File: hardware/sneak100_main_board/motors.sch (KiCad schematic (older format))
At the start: 16 parts, among them J1 Conn_01x06, J2 Conn_01x06, J3 Conn_01x06, J4 Conn_01x06, U1 DRV8835, U2 DRV8835, U3 DRV8835, U4 DRV8835

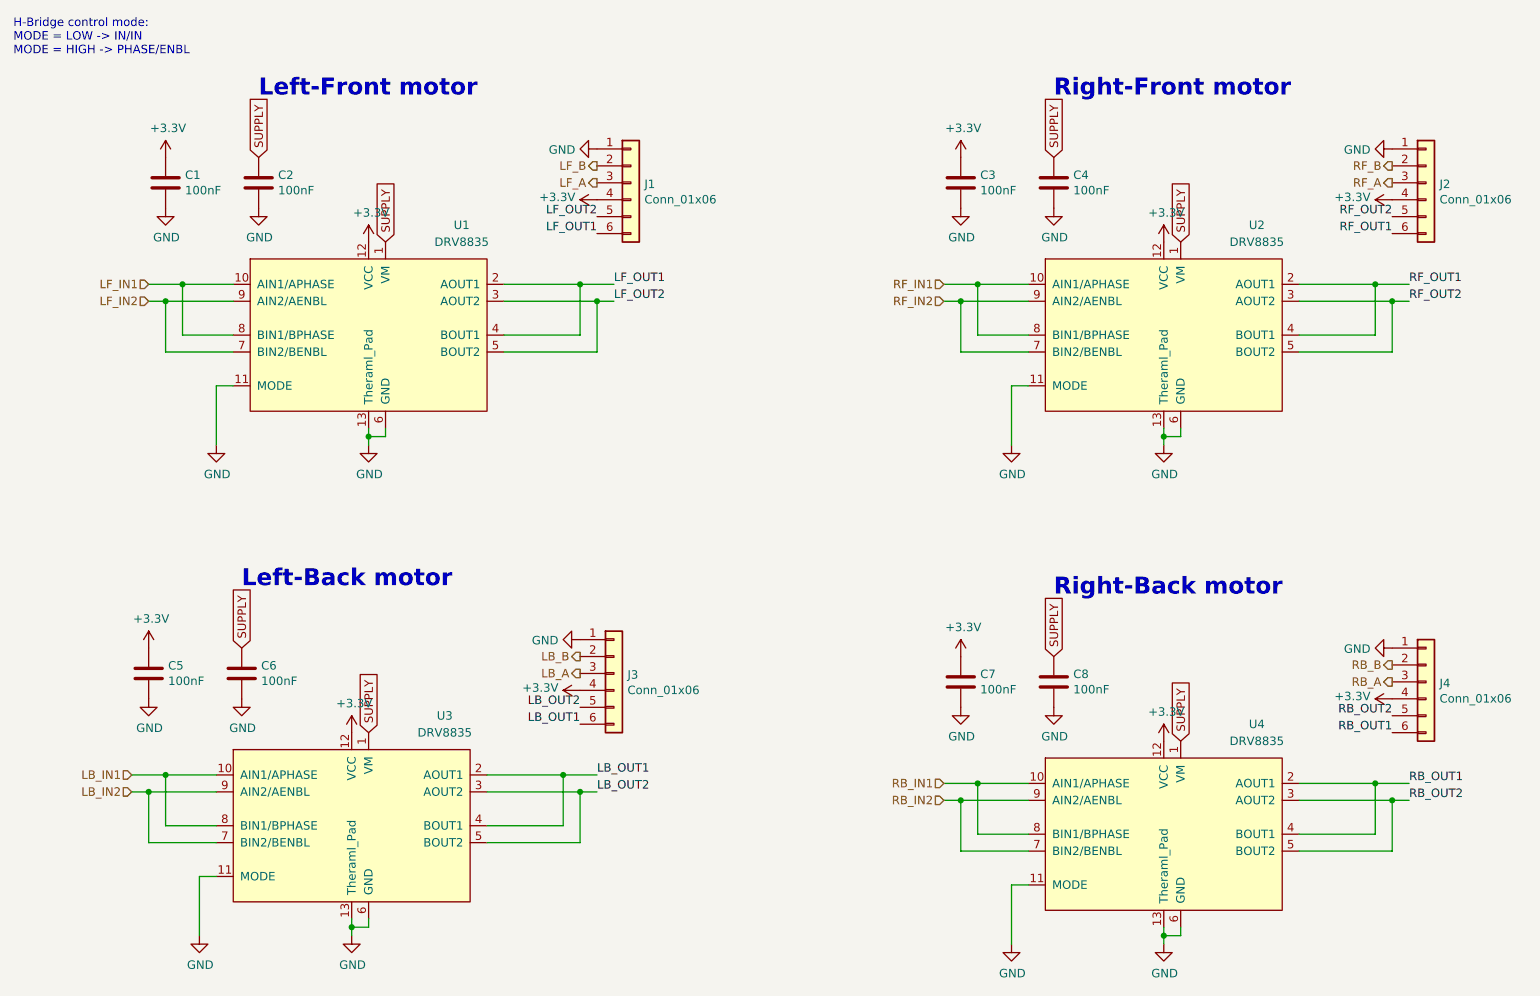
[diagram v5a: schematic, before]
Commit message: PCB first full layout
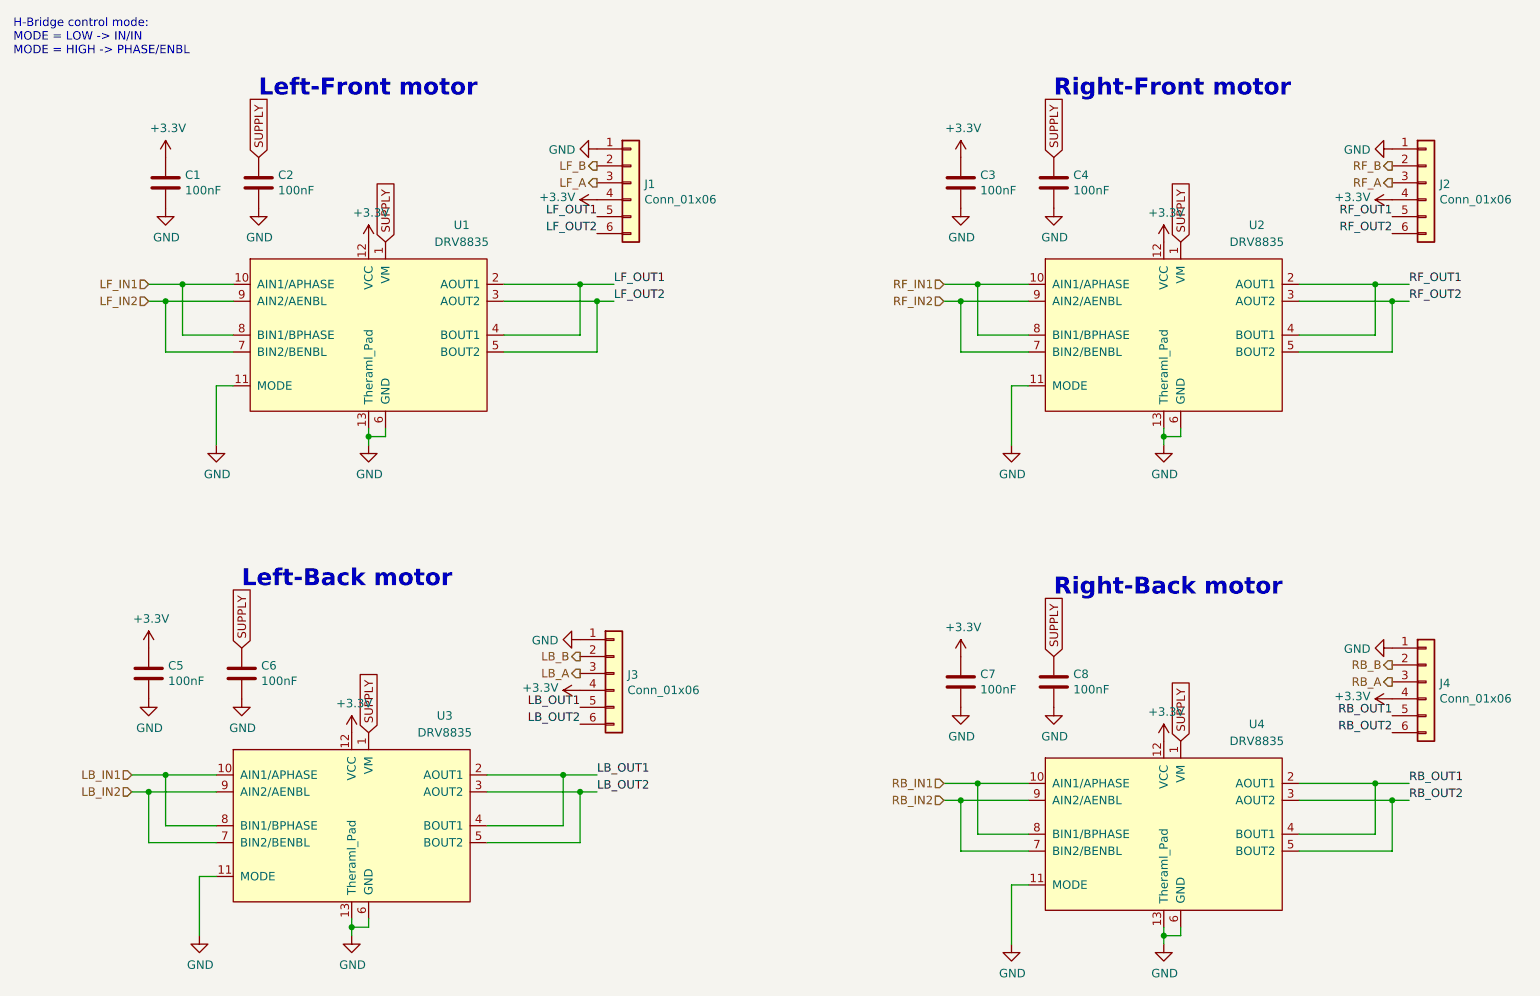
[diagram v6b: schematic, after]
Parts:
- J1, J2, J3, J4: footprint Connector_JST:JST_PH_S6B-PH-K_1x06_P2.00mm_Horizontal -> Connector_PinSocket_2.54mm:PinSocket_1x06_P2.54mm_Horizontal
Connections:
- net LB_OUT1: now also J3.5 (Pin_5); no longer J3.6 (Pin_6)
- net LB_OUT2: now also J3.6 (Pin_6); no longer J3.5 (Pin_5)
- net LF_OUT1: now also J1.5 (Pin_5); no longer J1.6 (Pin_6)
- net LF_OUT2: now also J1.6 (Pin_6); no longer J1.5 (Pin_5)
- net RB_OUT1: now also J4.5 (Pin_5); no longer J4.6 (Pin_6)
- net RB_OUT2: now also J4.6 (Pin_6); no longer J4.5 (Pin_5)
- net RF_OUT1: now also J2.5 (Pin_5); no longer J2.6 (Pin_6)
- net RF_OUT2: now also J2.6 (Pin_6); no longer J2.5 (Pin_5)
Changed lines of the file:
@@
 F 0 "J1" H 4630 1642 50  0000 L CNN
 F 1 "Conn_01x06" H 4630 1551 50  0000 L CNN
-F 2 "Connector_JST:JST_PH_S6B-PH-K_1x06_P2.00mm_Horizontal" H 4550 1650 50  0001 C CNN
+F 2 "Connector_PinSocket_2.54mm:PinSocket_1x06_P2.54mm_Horizontal" H 4550 1650 50  0001 C CNN
 F 3 "~" H 4550 1650 50  0001 C CNN
 	1    4550 1650
@@
 	0    -1   -1   0
 $EndComp
+Text Label 4350 1850 2    50   ~ 0
+LF_OUT1
 Text Label 4350 1950 2    50   ~ 0
-LF_OUT1
-Text Label 4350 1850 2    50   ~ 0
 LF_OUT2
 Text HLabel 4350 1650 0    50   Output ~ 0
@@
 F 0 "J2" H 9330 1642 50  0000 L CNN
 F 1 "Conn_01x06" H 9330 1551 50  0000 L CNN
-F 2 "Connector_JST:JST_PH_S6B-PH-K_1x06_P2.00mm_Horizontal" H 9250 1650 50  0001 C CNN
+F 2 "Connector_PinSocket_2.54mm:PinSocket_1x06_P2.54mm_Horizontal" H 9250 1650 50  0001 C CNN
 F 3 "~" H 9250 1650 50  0001 C CNN
 	1    9250 1650
@@
 	0    -1   -1   0
 $EndComp
+Text Label 9050 1850 2    50   ~ 0
+RF_OUT1
 Text Label 9050 1950 2    50   ~ 0
-RF_OUT1
-Text Label 9050 1850 2    50   ~ 0
 RF_OUT2
 Text HLabel 9050 1650 0    50   Output ~ 0
@@
 F 0 "J3" H 4530 4542 50  0000 L CNN
 F 1 "Conn_01x06" H 4530 4451 50  0000 L CNN
-F 2 "Connector_JST:JST_PH_S6B-PH-K_1x06_P2.00mm_Horizontal" H 4450 4550 50  0001 C CNN
+F 2 "Connector_PinSocket_2.54mm:PinSocket_1x06_P2.54mm_Horizontal" H 4450 4550 50  0001 C CNN
 F 3 "~" H 4450 4550 50  0001 C CNN
 	1    4450 4550
@@
 	0    -1   -1   0
 $EndComp
+Text Label 4250 4750 2    50   ~ 0
+LB_OUT1
 Text Label 4250 4850 2    50   ~ 0
-LB_OUT1
-Text Label 4250 4750 2    50   ~ 0
 LB_OUT2
 Text HLabel 4250 4550 0    50   Output ~ 0
@@
 F 0 "J4" H 9330 4592 50  0000 L CNN
 F 1 "Conn_01x06" H 9330 4501 50  0000 L CNN
-F 2 "Connector_JST:JST_PH_S6B-PH-K_1x06_P2.00mm_Horizontal" H 9250 4600 50  0001 C CNN
+F 2 "Connector_PinSocket_2.54mm:PinSocket_1x06_P2.54mm_Horizontal" H 9250 4600 50  0001 C CNN
 F 3 "~" H 9250 4600 50  0001 C CNN
 	1    9250 4600
@@
 	0    -1   -1   0
 $EndComp
+Text Label 9050 4800 2    50   ~ 0
+RB_OUT1
 Text Label 9050 4900 2    50   ~ 0
-RB_OUT1
-Text Label 9050 4800 2    50   ~ 0
 RB_OUT2
 Text HLabel 9050 4600 0    50   Output ~ 0

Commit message: Add external proximity sensor, erase old from schematic
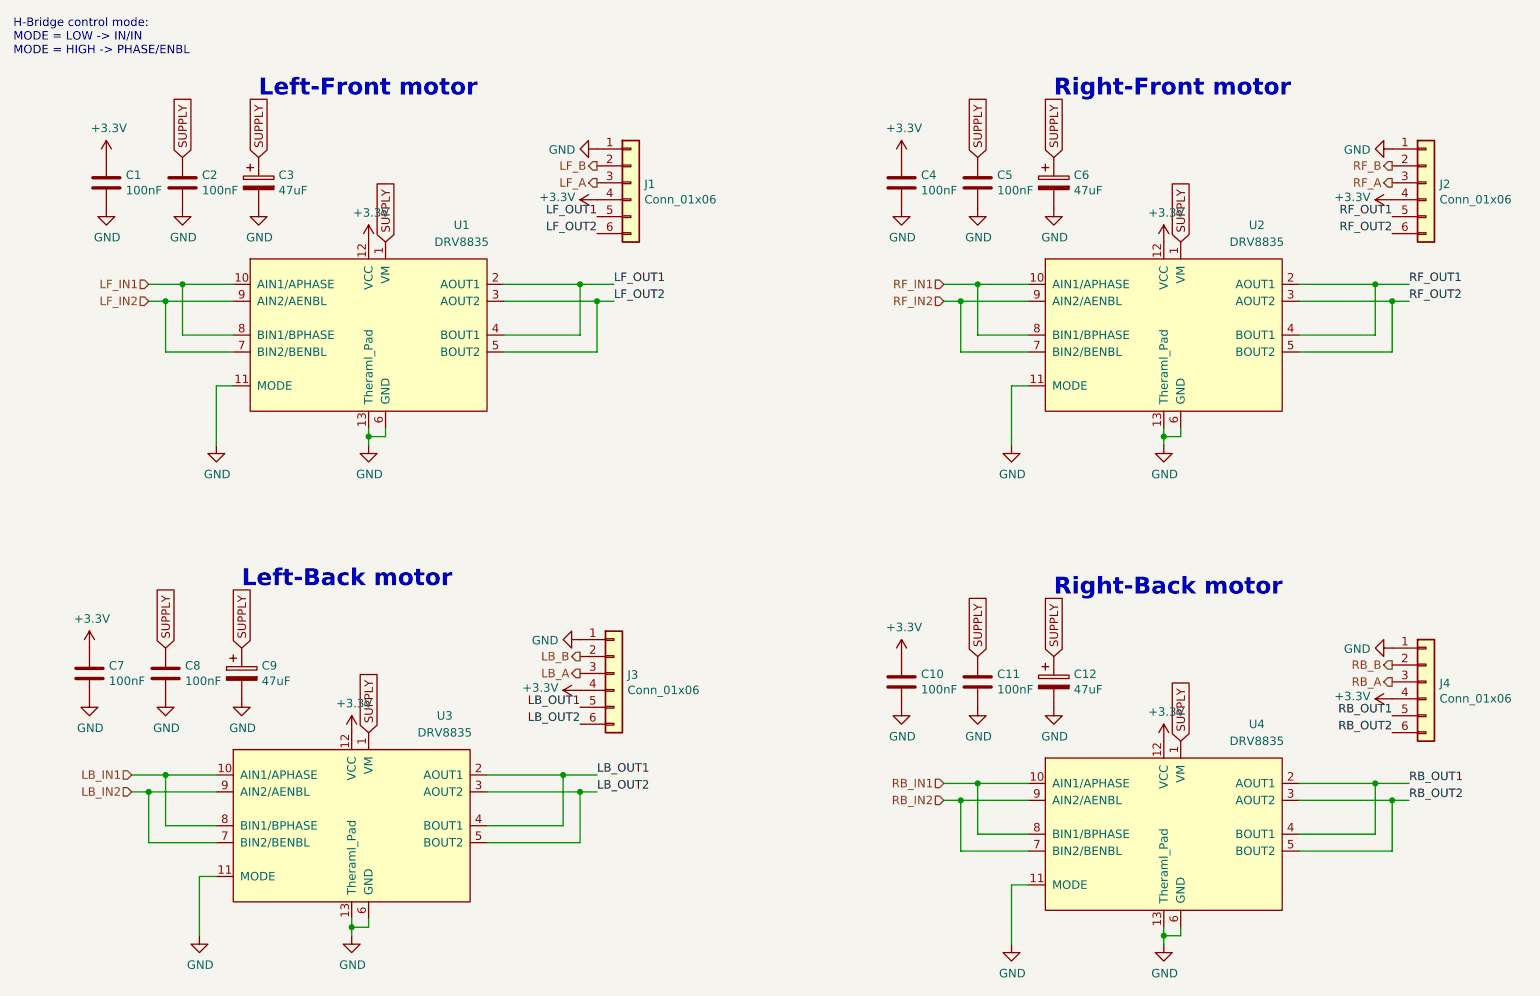
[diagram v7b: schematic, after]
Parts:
- added C12, C3, C6, C9: 47uF, Capacitor_Tantalum_SMD:CP_EIA-3216-18_Kemet-A, symbol Device:CP
- renumbered C7 to C10, C8 to C11, C3 to C4, C4 to C5, C5 to C7, C6 to C8
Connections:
- net GND: now also C12.2, C3.2, C6.2, C9.2
- net SUPPLY: now also C12.1, C3.1, C6.1, C9.1
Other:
- moved on the sheet: C1, C10, C11, C2, C4, C5, C7, C8

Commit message: Generate gerbers
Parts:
- U1, U2, U3, U4: footprint Package_SON:WSON-12-1EP_3x2mm_P0.5mm_EP1x2.65_ThermalVias -> sneak100_lib:DRV8835_hand_solder
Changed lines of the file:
@@
 F 0 "U1" H 3550 3000 50  0000 C CNN
 F 1 "DRV8835" H 3550 2900 50  0000 C CNN
-F 2 "Package_SON:WSON-12-1EP_3x2mm_P0.5mm_EP1x2.65_ThermalVias" H 2950 2900 50  0001 C CNN
+F 2 "sneak100_lib:DRV8835_hand_solder" H 2950 2900 50  0001 C CNN
 F 3 "" H 2950 2900 50  0001 C CNN
 	1    3050 2450
@@
 F 0 "U2" H 8250 3000 50  0000 C CNN
 F 1 "DRV8835" H 8250 2900 50  0000 C CNN
-F 2 "Package_SON:WSON-12-1EP_3x2mm_P0.5mm_EP1x2.65_ThermalVias" H 7650 2900 50  0001 C CNN
+F 2 "sneak100_lib:DRV8835_hand_solder" H 7650 2900 50  0001 C CNN
 F 3 "" H 7650 2900 50  0001 C CNN
 	1    7750 2450
@@
 F 0 "U3" H 3450 5900 50  0000 C CNN
 F 1 "DRV8835" H 3450 5800 50  0000 C CNN
-F 2 "Package_SON:WSON-12-1EP_3x2mm_P0.5mm_EP1x2.65_ThermalVias" H 2850 5800 50  0001 C CNN
+F 2 "sneak100_lib:DRV8835_hand_solder" H 2850 5800 50  0001 C CNN
 F 3 "" H 2850 5800 50  0001 C CNN
 	1    2950 5350
@@
 F 0 "U4" H 8250 5950 50  0000 C CNN
 F 1 "DRV8835" H 8250 5850 50  0000 C CNN
-F 2 "Package_SON:WSON-12-1EP_3x2mm_P0.5mm_EP1x2.65_ThermalVias" H 7650 5850 50  0001 C CNN
+F 2 "sneak100_lib:DRV8835_hand_solder" H 7650 5850 50  0001 C CNN
 F 3 "" H 7650 5850 50  0001 C CNN
 	1    7750 5400
